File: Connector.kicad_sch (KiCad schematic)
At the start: 1 part, among them P1 PCIEx4 EDGE CONNECTOR

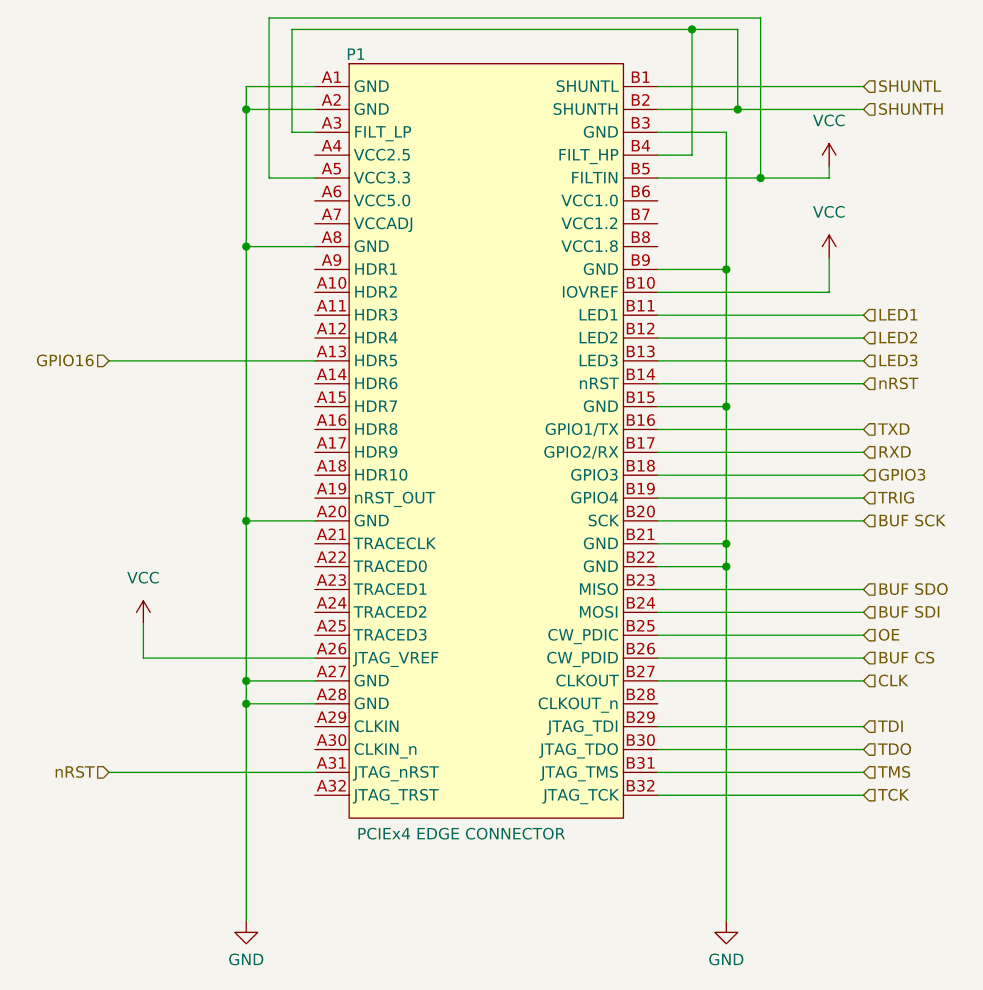
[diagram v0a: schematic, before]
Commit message: updated ESP32 design - needs silkscreen added and shunt should be moved to be closer to U1
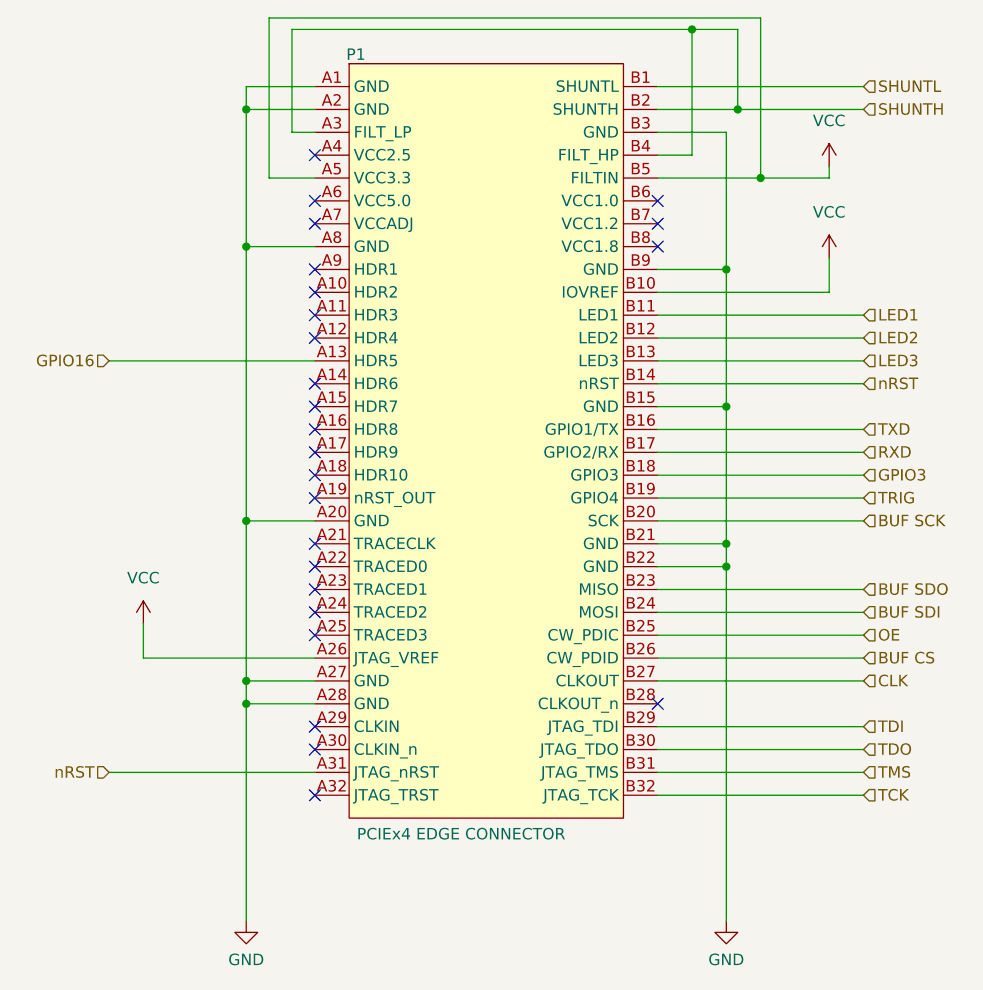
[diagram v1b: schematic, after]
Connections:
- no-connect marks 0 -> 25
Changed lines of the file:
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@@
 		(color 0 0 0 0)
+	)
+	(no_connect
+		(at 123.19 72.39)
+	)
+	(no_connect
+		(at 123.19 107.95)
+	)
+	(no_connect
+		(at 123.19 64.77)
+	)
+	(no_connect
+		(at 123.19 82.55)
+	)
+	(no_connect
+		(at 123.19 102.87)
+	)
+	(no_connect
+		(at 123.19 77.47)
+	)
+	(no_connect
+		(at 123.19 62.23)
+	)
+	(no_connect
+		(at 123.19 123.19)
+	)
+	(no_connect
+		(at 123.19 57.15)
+	)
+	(no_connect
+		(at 161.29 67.31)
+	)
+	(no_connect
+		(at 123.19 110.49)
+	)
+	(no_connect
+		(at 123.19 90.17)
+	)
+	(no_connect
+		(at 123.19 74.93)
+	)
+	(no_connect
+		(at 123.19 120.65)
+	)
+	(no_connect
+		(at 123.19 105.41)
+	)
+	(no_connect
+		(at 123.19 69.85)
+	)
+	(no_connect
+		(at 123.19 100.33)
+	)
+	(no_connect
+		(at 161.29 64.77)
+	)
+	(no_connect
+		(at 123.19 128.27)
+	)
+	(no_connect
+		(at 123.19 87.63)
+	)
+	(no_connect
+		(at 123.19 95.25)
+	)
+	(no_connect
+		(at 123.19 92.71)
+	)
+	(no_connect
+		(at 161.29 62.23)
+	)
+	(no_connect
+		(at 123.19 85.09)
+	)
+	(no_connect
+		(at 161.29 118.11)
 	)
 	(wire

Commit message: updated pcb and schematic after library re-organization, also updated header to the correct footprint
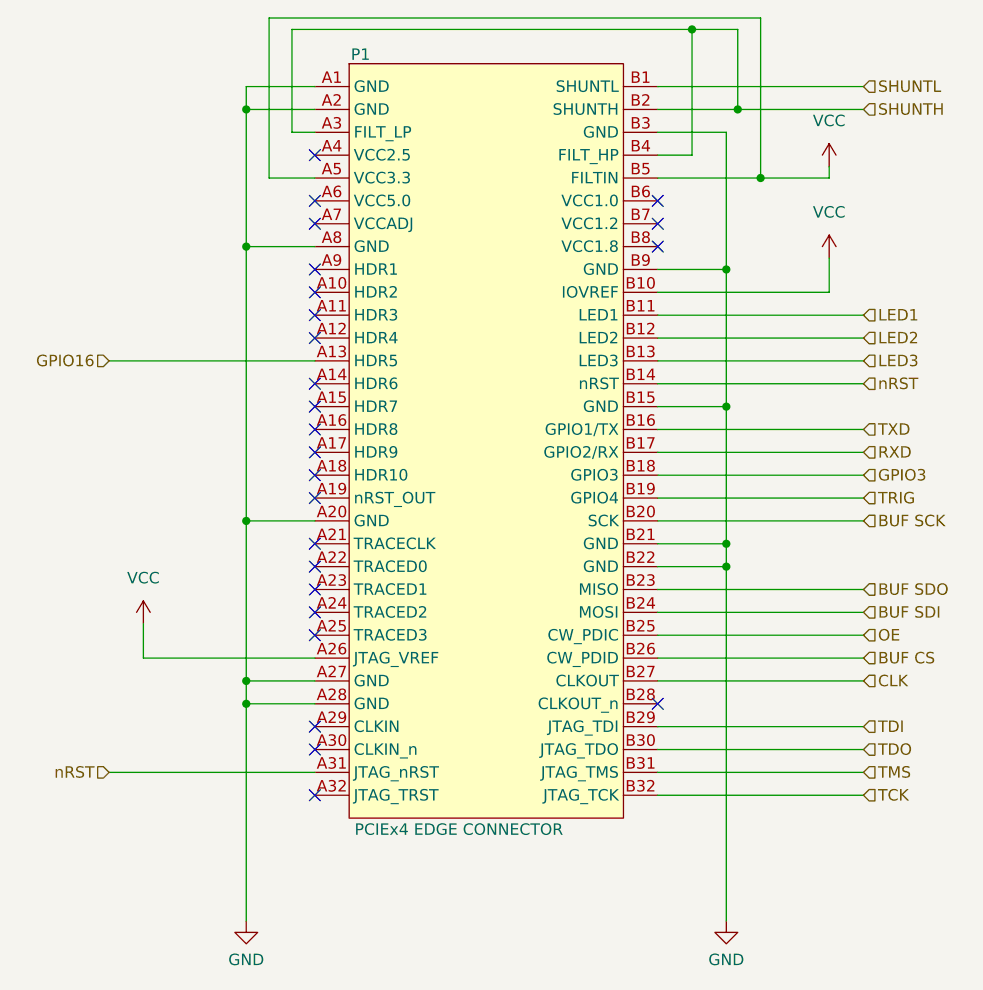
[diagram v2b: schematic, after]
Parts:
- removed P1: PCIEx4 EDGE CONNECTOR, tutorial_2_library:CW312_Template, symbol tutorial_2_library:CW312T-Template
- added P1: PCIEx4 EDGE CONNECTOR, tutorial_2_library:CW312_Template, symbol NAE_Connectors:CW312T-Template
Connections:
- net BUF CS: now also P1.B26 (CW_PDID)
- net BUF SCK: now also P1.B20 (SCK)
- net BUF SDI: now also P1.B24 (MOSI)
- net BUF SDO: now also P1.B23 (MISO)
- net CLK: now also P1.B27 (CLKOUT)
- net GND: now also P1.A1 (GND), P1.A2 (GND), P1.A20 (GND), P1.A27 (GND), P1.A28 (GND), P1.A8 (GND), P1.B15 (GND), P1.B21 (GND), P1.B22 (GND), P1.B3 (GND), P1.B9 (GND)
- net GPIO16: now also P1.A13 (HDR5)
- net GPIO3: now also P1.B18 (GPIO3)
- net LED1: now also P1.B11 (LED1)
- net LED2: now also P1.B12 (LED2)
- net LED3: now also P1.B13 (LED3)
- net OE: now also P1.B25 (CW_PDIC)
- net RXD: now also P1.B17 (GPIO2/RX)
- net SHUNTH: now also P1.A3 (FILT_LP), P1.B2 (SHUNTH), P1.B4 (FILT_HP)
- net SHUNTL: now also P1.B1 (SHUNTL)
- net TCK: now also P1.B32 (JTAG_TCK)
- net TDI: now also P1.B29 (JTAG_TDI)
- net TDO: now also P1.B30 (JTAG_TDO)
- net TMS: now also P1.B31 (JTAG_TMS)
- net TRIG: now also P1.B19 (GPIO4)
- net TXD: now also P1.B16 (GPIO1/TX)
- net VCC: now also P1.A26 (JTAG_VREF), P1.A5 (VCC3.3), P1.B10 (IOVREF), P1.B5 (FILTIN)
- net nRST: now also P1.A31 (JTAG_nRST), P1.B14 (nRST)
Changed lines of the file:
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@@
-	)
-	(symbol
-		(lib_id "tutorial_2_library:CW312T-Template")
-		(at 142.24 49.53 0)
-		(unit 1)
-		(exclude_from_sim no)
-		(in_bom no)
-		(on_board yes)
-		(dnp no)
-		(property "Reference" "P1"
-			(at 127.762 45.974 0)
-			(effects
-				(font
-					(size 1.27 1.27)
-				)
-			)
-		)
-		(property "Value" "PCIEx4 EDGE CONNECTOR"
-			(at 139.446 132.588 0)
-			(effects
-				(font
-					(size 1.27 1.27)
-				)
-			)
-		)
-		(property "Footprint" "tutorial_2_library:CW312_Template"
-			(at 138.43 142.24 0)
-			(effects
-				(font
-					(size 1.27 1.27)
-				)
-				(hide yes)
-			)
-		)
-		(property "Datasheet" ""
-			(at 139.7 48.26 0)
-			(effects
-				(font
-					(size 1.27 1.27)
-				)
-				(hide yes)
-			)
-		)
-		(property "Description" "BOARD AND EDGE CONNECTOR TEMPLATE FOR CW312 TARGETS"
-			(at 151.13 138.43 0)
-			(effects
-				(font
-					(size 1.27 1.27)
-				)
-				(hide yes)
-			)
-		)
-		(pin "A30"
-		)
-		(pin "A24"
-		)
-		(pin "B19"
-		)
-		(pin "B25"
-		)
-		(pin "B3"
-		)
-		(pin "B18"
-		)
-		(pin "A10"
-		)
-		(pin "A14"
-		)
-		(pin "A21"
-		)
-		(pin "A15"
-		)
-		(pin "A16"
-		)
-		(pin "A22"
-		)
-		(pin "A3"
-		)
-		(pin "A6"
-		)
-		(pin "A23"
-		)
-		(pin "A7"
-		)
-		(pin "A2"
-		)
-		(pin "A4"
-		)
-		(pin "B1"
-		)
-		(pin "B11"
-		)
-		(pin "A8"
-		)
-		(pin "B13"
-		)
-		(pin "B14"
-		)
-		(pin "A28"
-		)
-		(pin "B17"
-		)
-		(pin "A1"
-		)
-		(pin "B10"
-		)
-		(pin "B2"
-		)
-		(pin "B20"
-		)
-		(pin "B21"
-		)
-		(pin "A19"
-		)
-		(pin "A27"
-		)
-		(pin "A32"
-		)
-		(pin "B22"
-		)
-		(pin "A25"
-		)
-		(pin "B12"
-		)
-		(pin "B23"
-		)
-		(pin "A13"
-		)
-		(pin "A20"
-		)
-		(pin "A5"
-		)
-		(pin "A29"
-		)
-		(pin "A26"
-		)
-		(pin "B24"
-		)
-		(pin "B28"
-		)
-		(pin "B29"
-		)
-		(pin "B30"
-		)
-		(pin "B31"
-		)
-		(pin "B15"
-		)
-		(pin "A12"
-		)
-		(pin "A18"
-		)
-		(pin "A31"
-		)
-		(pin "A9"
-		)
-		(pin "B16"
-		)
-		(pin "B26"
-		)
-		(pin "A11"
-		)
-		(pin "B27"
-		)
-		(pin "B32"
-		)
-		(pin "B4"
-		)
-		(pin "B5"
-		)
-		(pin "A17"
-		)
-		(pin "B6"
-		)
-		(pin "B9"
-		)
-		(pin "B8"
-		)
-		(pin "B7"
-		)
-		(instances
-			(project "KiCAD_Test3"
-				(path "/3a5d4ac2-6e78-4735-b22c-b99217f3b036/bdf9dfe7-ebbc-4e1b-a7b9-19e8a6ddc3c1"
-					(reference "P1")
-					(unit 1)
-				)
-			)
-		)
 	)
 	(symbol
@@
 					(unit 1)
 				)
+			)
+		)
+	)
+	(symbol
+		(lib_id "NAE_Connectors:CW312T-Template")
+		(at 142.24 49.53 0)
+		(unit 1)
+		(exclude_from_sim no)
+		(in_bom no)
+		(on_board yes)
+		(dnp no)
+		(property "Reference" "P1"
+			(at 128.27 45.974 0)
+			(effects
+				(font
+					(size 1.27 1.27)
+				)
+			)
+		)
+		(property "Value" "PCIEx4 EDGE CONNECTOR"
+			(at 139.192 132.08 0)
+			(effects
+				(font
+					(size 1.27 1.27)
+				)
+			)
+		)
+		(property "Footprint" "tutorial_2_library:CW312_Template"
+			(at 138.43 142.24 0)
+			(effects
+				(font
+					(size 1.27 1.27)
+				)
+				(hide yes)
+			)
+		)
+		(property "Datasheet" ""
+			(at 139.7 48.26 0)
+			(effects
+				(font
+					(size 1.27 1.27)
+				)
+				(hide yes)
+			)
+		)
+		(property "Description" "BOARD AND EDGE CONNECTOR TEMPLATE FOR CW312 TARGETS"
+			(at 151.13 138.43 0)
+			(effects
+				(font
+					(size 1.27 1.27)
+				)
+				(hide yes)
+			)
+		)
+		(pin "A21"
+		)
+		(pin "A5"
+		)
+		(pin "A9"
+		)
+		(pin "A10"
+		)
+		(pin "B17"
+		)
+		(pin "B21"
+		)
+		(pin "B20"
+		)
+		(pin "A2"
+		)
+		(pin "B15"
+		)
+		(pin "A1"
+		)
+		(pin "A27"
+		)
+		(pin "B22"
+		)
+		(pin "B23"
+		)
+		(pin "B25"
+		)
+		(pin "B18"
+		)
+		(pin "B16"
+		)
+		(pin "B27"
+		)
+		(pin "B28"
+		)
+		(pin "A17"
+		)
+		(pin "B24"
+		)
+		(pin "A23"
+		)
+		(pin "A20"
+		)
+		(pin "A11"
+		)
+		(pin "A15"
+		)
+		(pin "A18"
+		)
+		(pin "A25"
+		)
+		(pin "B11"
+		)
+		(pin "B12"
+		)
+		(pin "B13"
+		)
+		(pin "A12"
+		)
+		(pin "A14"
+		)
+		(pin "B26"
+		)
+		(pin "B29"
+		)
+		(pin "B3"
+		)
+		(pin "B19"
+		)
+		(pin "B1"
+		)
+		(pin "B30"
+		)
+		(pin "B32"
+		)
+		(pin "A28"
+		)
+		(pin "A7"
+		)
+		(pin "A4"
+		)
+		(pin "A19"
+		)
+		(pin "B31"
+		)
+		(pin "B4"
+		)
+		(pin "B5"
+		)
+		(pin "B6"
+		)
+		(pin "B7"
+		)
+		(pin "B8"
+		)
+		(pin "B2"
+		)
+		(pin "A16"
+		)
+		(pin "A13"
+		)
+		(pin "A32"
+		)
+		(pin "B14"
+		)
+		(pin "A26"
+		)
+		(pin "A30"
+		)
+		(pin "B10"
+		)
+		(pin "A6"
+		)
+		(pin "A29"
+		)
+		(pin "A22"
+		)
+		(pin "A31"
+		)
+		(pin "A24"
+		)
+		(pin "A3"
+		)
+		(pin "A8"
+		)
+		(pin "B9"
+		)
+		(instances
+			(project ""
+				(path "/3a5d4ac2-6e78-4735-b22c-b99217f3b036/bdf9dfe7-ebbc-4e1b-a7b9-19e8a6ddc3c1"
+					(reference "P1")
+					(unit 1)
+				)
